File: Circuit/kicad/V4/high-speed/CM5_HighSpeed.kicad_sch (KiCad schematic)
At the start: 20 parts, among them J11 THD-02-R, J2 USB3_A, J3 690-019-298-412, J4 690-019-298-412, U1 AP22653W6, U2 RT9742SNGV

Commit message: high speed first step
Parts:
- renumbered C5 to C4, C6 to C5, C1 to C6, C2 to C7, C3 to C8, C4 to C9, J3 to J2, J2 to J3, J11 to J4, J4 to J5, R3 to R1, R4 to R2, R2 to R3, R1 to R4, TP4 to TP1, U2 to U1, U1 to U2

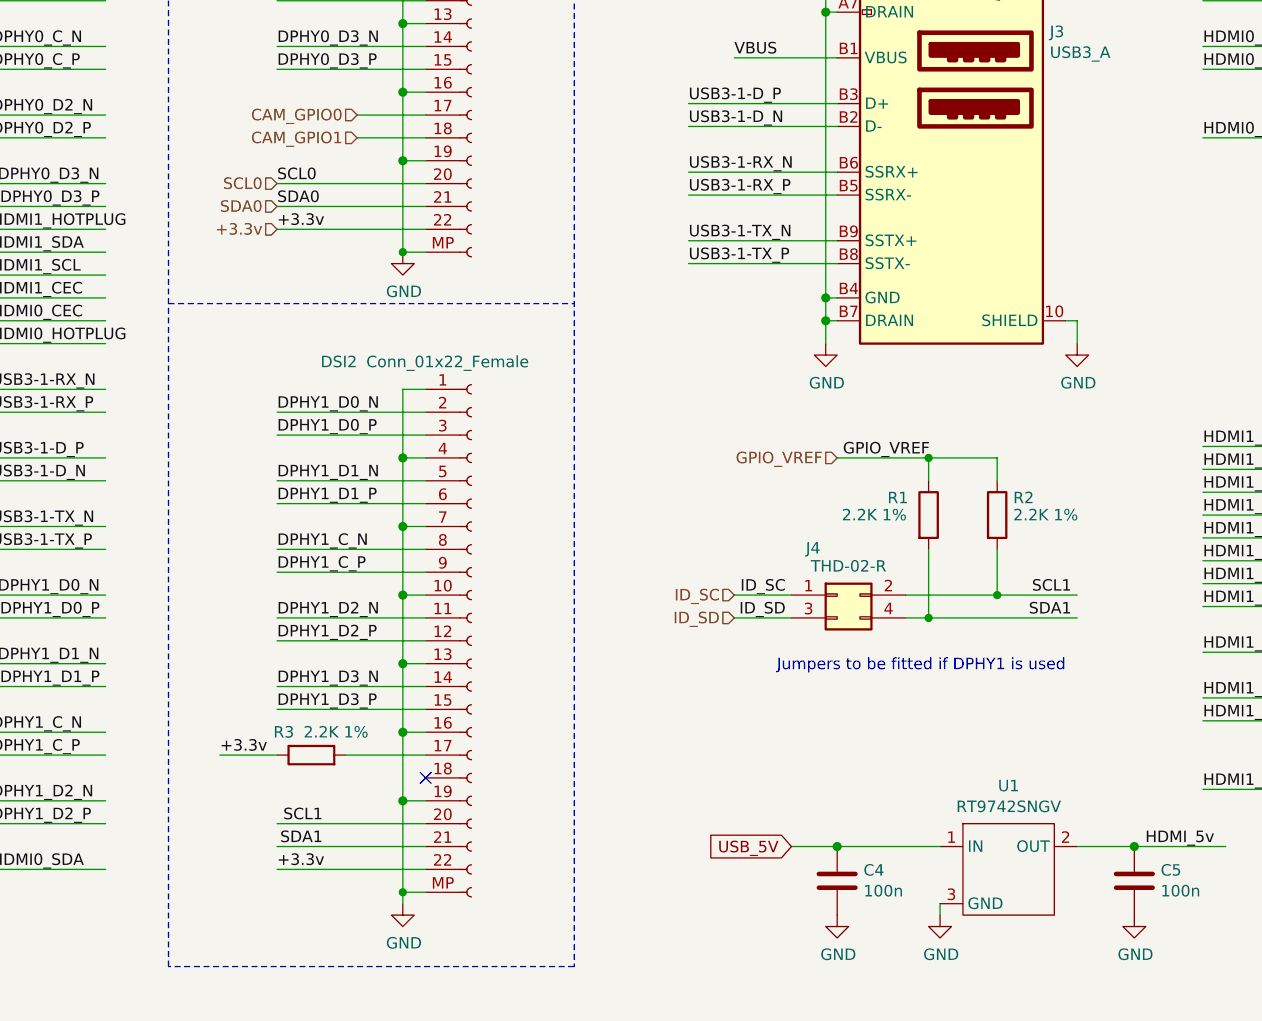
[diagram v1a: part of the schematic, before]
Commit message: added psu start delay rc tag, high speed first inner and outboard impedance calculations
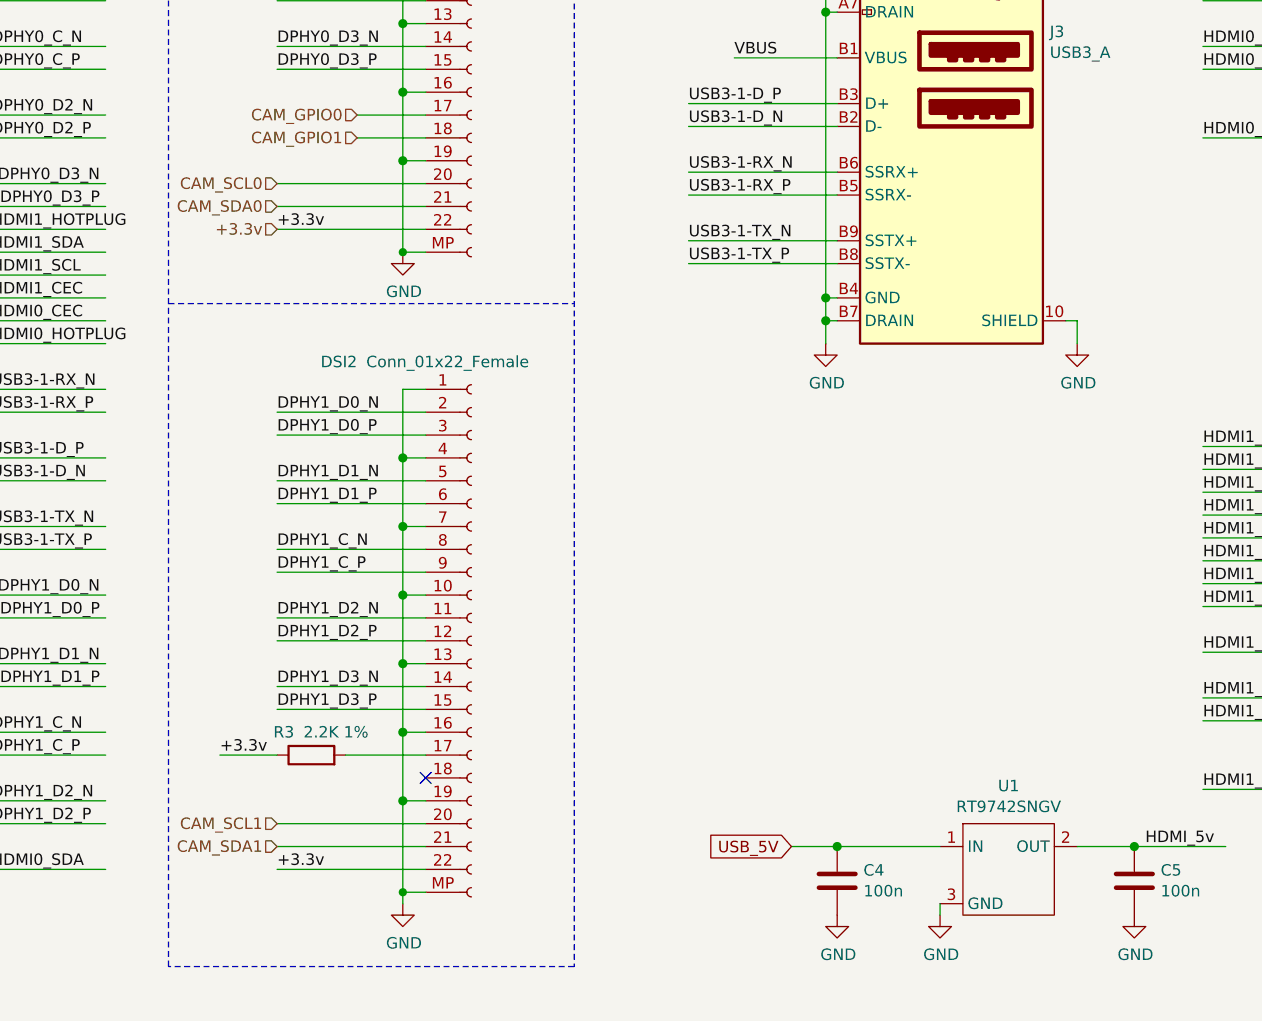
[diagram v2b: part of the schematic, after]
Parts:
- removed J4: THD-02-R, Connector_PinHeader_2.54mm:PinHeader_2x02_P2.54mm_Vertical, symbol Connector_Generic:Conn_02x02_Odd_Even
- removed R1, R2: 2.2K 1%, Resistor_SMD:R_0805_2012Metric, symbol Device:R
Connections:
- net SCL0 renamed CAM_SCL0
- net SCL1 renamed CAM_SCL1
- net SDA0 renamed CAM_SDA0
- net SDA1 renamed CAM_SDA1
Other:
- note removed: "Jumpers to be fitted if DPHY1 is used"

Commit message: kicad: high speed V2.2 Circuit finish psu bom update
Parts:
- C10: renamed from C7; Cikkszám (none) -> 100.286.19; Field4 Mouser -> (none); Field5 667-EEF-CX0J101R -> (none); Field7 Panasonic -> (none); Link (none) -> https://www.hestore.hu/prod_10028619.html; Part Description Capacitor, SP-Cap, 100u, 6.3V, 15mR ESR -> (none)
- C11: renamed from C8; value 10u -> 10uF; Cikkszám (none) -> 100.230.37; Field4 Digikey -> (none); Field5 490-14381-1-ND -> (none); Field6 GRM21BR71A106KA73L -> (none); Field7 Murata -> (none); Field8 111893011 -> (none); Link (none) -> https://www.hestore.hu/prod_10023037.html; Part Description 10uF 10% 10V Ceramic Capacitor X7R 0805 (2012 Metric) -> (none)
- C12: renamed from C9; value 10u -> 10uF; Cikkszám (none) -> 100.230.37; Field4 Digikey -> (none); Field5 490-14381-1-ND -> (none); Field6 GRM21BR71A106KA73L -> (none); Field7 Murata -> (none); Field8 111893011 -> (none); Link (none) -> https://www.hestore.hu/prod_10023037.html; Part Description 10uF 10% 10V Ceramic Capacitor X7R 0805 (2012 Metric) -> (none)
- C7: renamed from C4; value 100n -> 100nf; Cikkszám (none) -> 100.011.22; Field4 Farnell -> (none); Field5 2611911 -> (none); Field6 RM EMK105 B7104KV-F -> (none); Field7 TAIYO YUDEN EUROPE GMBH -> (none); Field8 110091611 -> (none); Link (none) -> https://www.hestore.hu/prod_10001122.html; Part Description 0.1uF 10% 16V Ceramic Capacitor X7R 0402 (1005 Metric) -> (none)
- C8: renamed from C5; value 100n -> 100nf; Cikkszám (none) -> 100.011.22; Field4 Farnell -> (none); Field5 2611911 -> (none); Field6 RM EMK105 B7104KV-F -> (none); Field7 TAIYO YUDEN EUROPE GMBH -> (none); Field8 110091611 -> (none); Link (none) -> https://www.hestore.hu/prod_10001122.html; Part Description 0.1uF 10% 16V Ceramic Capacitor X7R 0402 (1005 Metric) -> (none)
- C9: renamed from C6; value 10u -> 10uF; Cikkszám (none) -> 100.230.37; Field4 Digikey -> (none); Field5 490-14381-1-ND -> (none); Field6 GRM21BR71A106KA73L -> (none); Field7 Murata -> (none); Field8 111893011 -> (none); Link (none) -> https://www.hestore.hu/prod_10023037.html; Part Description 10uF 10% 10V Ceramic Capacitor X7R 0805 (2012 Metric) -> (none)
- DSI1, DSI2: Cikkszám (none) -> 100.460.85; Field4 Mouser -> (none); Field5 798-FH12-22S-0.5SH55 -> (none); Field6 FH12-22S-0.5SH55 -> (none); Field7 Hirose -> (none); Link (none) -> https://www.hestore.hu/prod_10046085.html; Part Description 22 Position FFC, FPC Connector Contacts, Bottom 0.020" (0.5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 -> (none)
- J3: renamed from J2; value 690-019-298-412 -> HDMI; footprint psu:EDAC 690-019-298-412 -> panel:EDAC 690-019-298-412; Cikkszám (none) -> 100.303.99; Field4 Farnell -> (none); Field5 2614936 -> (none); Field6 690-019-298-412 -> (none); Field7 EDAC -> (none); Field8 UCON00802 -> (none); Link (none) -> https://www.hestore.hu/prod_10030399.html; Part Description HDMI Connector, Right Angle, 19 Contacts, Receptacle, Surfa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 -> (none)
- J4: renamed from J3; footprint psu:MTCONN_UBAF30-D2011 -> panel:MTCONN_UBAF30-D2011; Cikkszám (none) -> 100.491.29; Field5 UBAF30-D2011 -> (none); Field6 UBAF30-D2011 -> (none); Field7 Mtconn -> (none); Link (none) -> https://www.hestore.hu/prod_10049129.html; Part Description Dual USB 3 connector -> (none)
- J5: value 690-019-298-412 -> HDMI; footprint psu:EDAC 690-019-298-412 -> panel:EDAC 690-019-298-412; Cikkszám (none) -> 100.303.99; Field4 Farnell -> (none); Field5 2614936 -> (none); Field6 690-019-298-412 -> (none); Field7 EDAC -> (none); Field8 UCON00802 -> (none); Link (none) -> https://www.hestore.hu/prod_10030399.html; Part Description HDMI Connector, Right Angle, 19 Contacts, Receptacle, Surfa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 -> (none)
- Module1: footprint psu:Raspberry-Pi-5-Compute-Module -> panel:Raspberry-Pi-5-Compute-Module; Cikkszám (none) -> 100.490.93; Field4 Amphenol -> (none); Field5 2x 10164227-1001A1RLF -> (none); Field6 2x 10164227-1001A1RLF -> (none); Field7 Hirose -> (none); Link (none) -> https://www.hestore.hu/prod_10049093.html; Part Description 100 Position Connector Receptacle, Center Strip Contacts Su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 -> (none)
- R5: renamed from R3; value 2.2K 1% -> 2.2K; Cikkszám (none) -> 100.406.77; Field4 Farnell -> (none); Link (none) -> https://www.hestore.hu/prod_10040677.html; Part Description Resistor 2.2K M1005 1% 63mW -> (none)
- R6: renamed from R4; value 15K 1% -> 15K; Cikkszám (none) -> 100.437.82; Field4 Farnell -> (none); Field5 9239375 -> (none); Field6 MCR01MZPF1502 -> (none); Field7 Rohm -> (none); Field8 120891581 -> (none); Link (none) -> https://www.hestore.hu/prod_10043782.html; Part Description Resistor 15K M1005 1% 63mW -> (none)
- TP1: Cikkszám (none) -> -; Link (none) -> -; now left out of the parts list
- U2: renamed from U1; Cikkszám (none) -> 100.490.97; Field4 Farnell -> (none); Field5 2575555 -> (none); Field6 RT9742SNGV -> (none); Field7 RichTek -> (none); Field8 USWI00155 -> (none); Link (none) -> https://www.hestore.hu/prod_10049097.html; Part Description Power Switch/Driver 1:1 N-Channel 500mA SOT-23-3 -> (none)
- U3: renamed from U2; Cikkszám (none) -> 100.460.82; Field4 Digikey -> (none); Field5 31-AP22653W6-7CT-ND -> (none); Field6 AP22653W6 -> (none); Field7 Diodes -> (none); Link (none) -> https://www.hestore.hu/prod_10046082.html; Part Description Power Switch/Driver 1:1 P-Channel 2.1A SOT-23-6 -> (none)
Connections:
- net CAM_SCL0 renamed CAM0_SCL
- net CAM_SCL1 renamed CAM1_SCL
- net CAM_SDA0 renamed CAM0_SDA
- net CAM_SDA1 renamed CAM1_SDA
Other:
- note added: "Gyári kapcsolásban sincs használva a fault, nem probléma ha nem megy ugyis észreveszem"

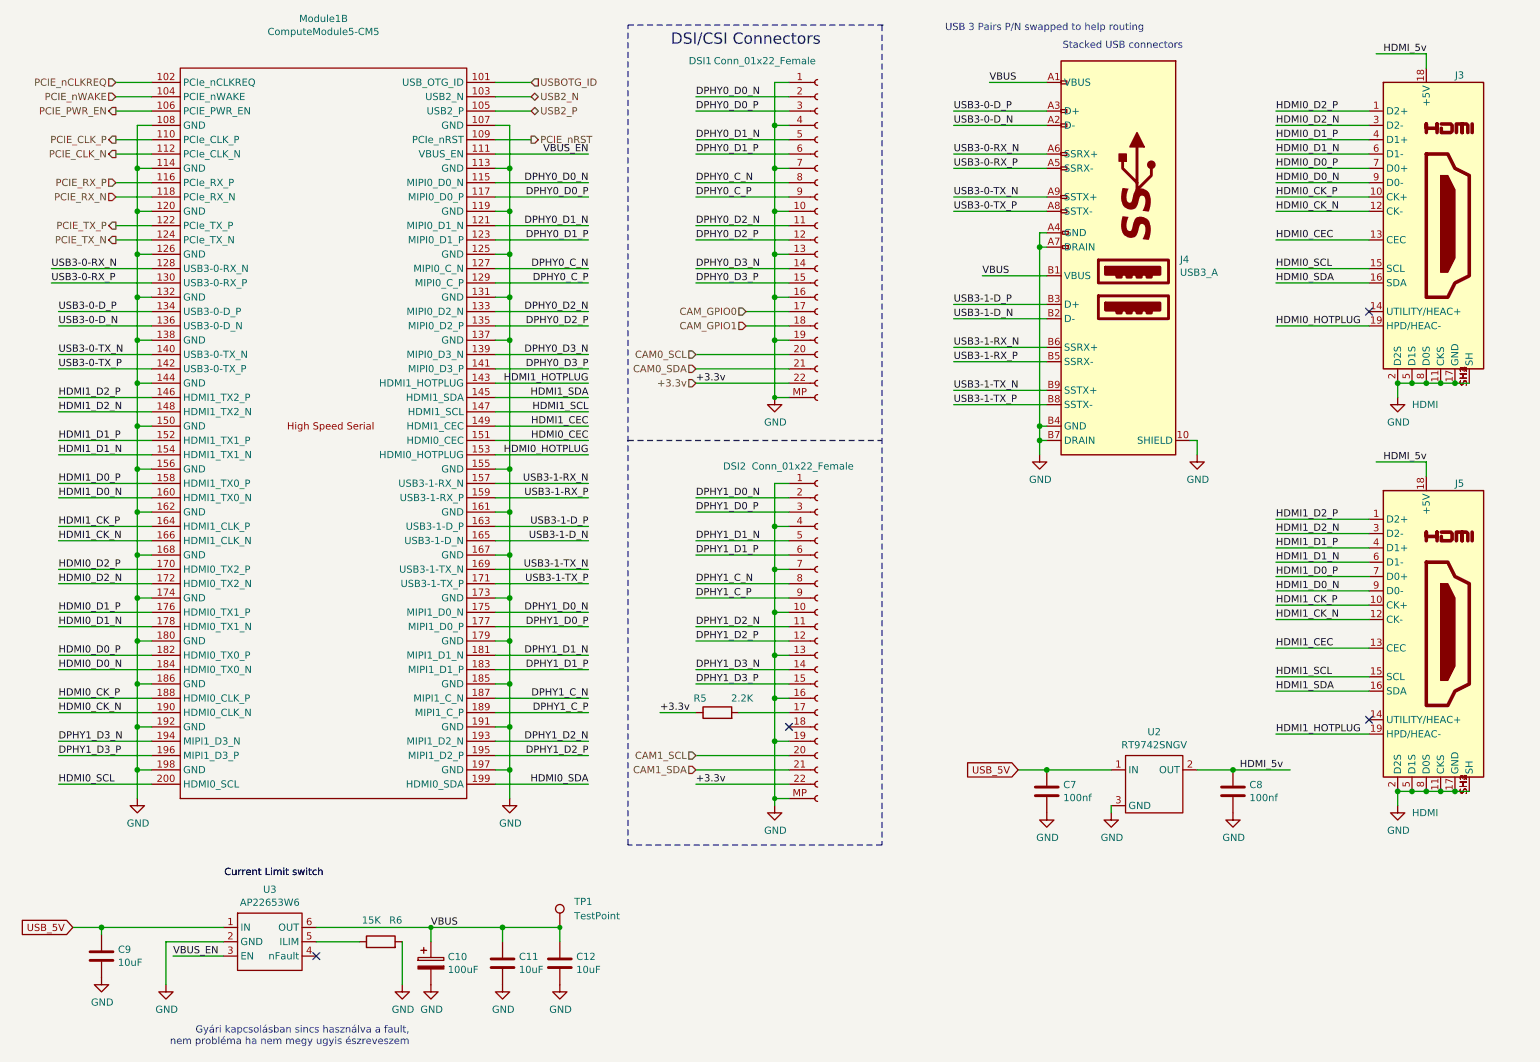
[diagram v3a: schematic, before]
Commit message: finished high-speed panel schematic and first try to doute gpios
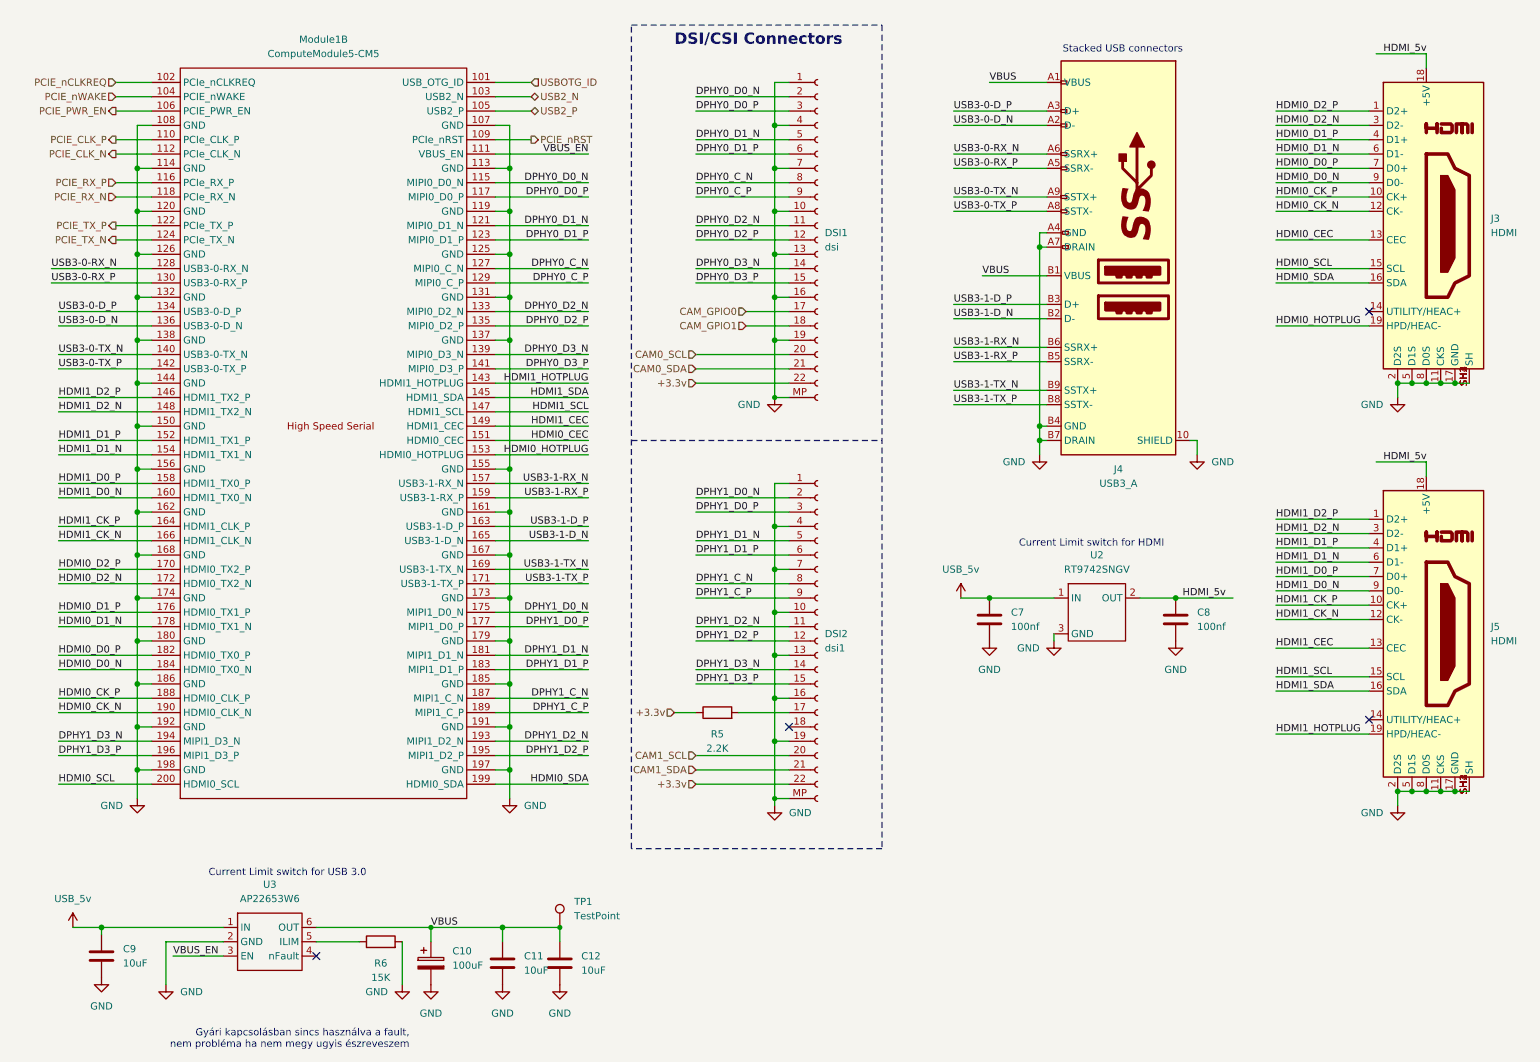
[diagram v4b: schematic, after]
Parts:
- C10: footprint Capacitor_Tantalum_SMD:CP_EIA-7343-31_Kemet-D -> Capacitor_Tantalum_SMD:CP_EIA-3528-21_Kemet-B
- C11, C12, C9: footprint Capacitor_Tantalum_SMD:CP_EIA-3528-21_Kemet-B -> Capacitor_Tantalum_SMD:CP_EIA-3216-18_Kemet-A_HandSolder
- DSI1: value Conn_01x22_Female -> dsi
- DSI2: value Conn_01x22_Female -> dsi1
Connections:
- net USB_5V renamed USB_5v
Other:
- note added: "Current Limit switch for HDMI"
- note added: "Current Limit switch for USB 3.0"
- note removed: "Current Limit switch"
- note removed: "USB 3 Pairs P/N swapped to help routing"
- moved on the sheet: C7, C8, U2

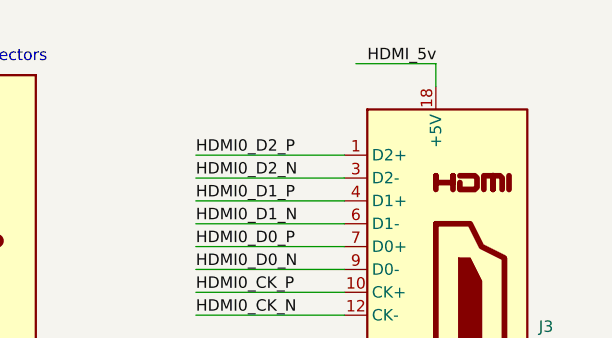
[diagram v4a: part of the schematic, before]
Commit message: High Speed all routed, DRC, DFM shows 0 error (without silkscreen layers)
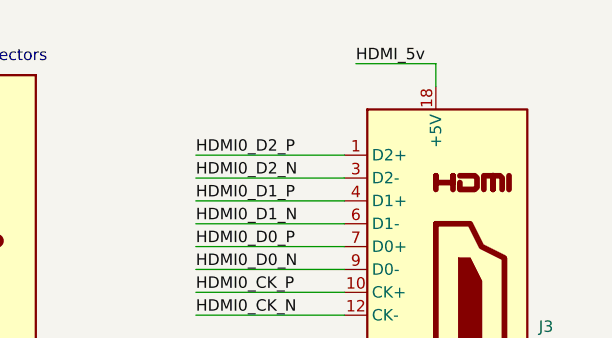
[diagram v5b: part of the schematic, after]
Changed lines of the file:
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@@
 	)
 	(label "HDMI_5v"
-		(at 256.54 20.32 0)
+		(at 255.27 20.32 0)
 		(effects
 			(font
